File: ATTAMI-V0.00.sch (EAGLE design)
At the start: 25 parts, among them U1 MIC5225, U2 ATTINY85-20SU, U3 1117

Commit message: a versin without the fancy LDO and SOT0232 for the X1117
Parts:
- removed COIN_CELL_(+): (no value), ATtami:PINHD-1X1
- removed D5: Schottky, ATtami:SCHOTTKY-DIODESOD-323
- removed U1: MIC5225, ATtami:V_REG_LDOSMD
- U3: device ATtami:XXX1117 -> ATtami:XXX1117SOT-232
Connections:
- removed net N$4: COIN_CELL_(+).1, D5.A
- net GND: no longer U1.GND
- net VCC: no longer D5.C, U1.OUT
- net V_BAT: no longer U1.EN, U1.IN
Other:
- note added: "Notes: 1. profit!! 2. Cut jumper SJ1 in order to save battery energy. 3. Switch possition of midi jumper and dissable the RESET function in order to use PB5 as DP USB signal. 4. D1 and D2 are Blue LEDs their forward voltage is 3.2V. They might not light when using coin cell or low Vi_BAT. 5. When VCC is less than 5V the system clock of the ATTINY85 should be 8MHz or less (refer to the datasheet P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"
- note added: "this is/was coincell +"
- note removed: "* See Note 1"
- note removed: "Notes: 1. Assemble either U1 or U3. (!!! never both of them !!!) 2. Cut jumper SJ1 in order to save battery energy. 3. Switch possition of midi jumper and dissable the RESET function in order to use PB5 as DP USB signal. 4. D1 and D2 are Blue LEDs their forward voltage is 3.2V. They might not light when using coin cell or low Vi_BAT. 5. When VCC is less than 5V the system clock of the ATTINY85 sh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"
- moved on the sheet: U3
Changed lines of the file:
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@@
 <layer number="19" name="Unrouted" color="6" fill="1" visible="no" active="no"/>
 <layer number="20" name="Dimension" color="15" fill="1" visible="no" active="no"/>
-<layer number="21" name="tPlace" color="7" fill="1" visible="no" active="no"/>
-<layer number="22" name="bPlace" color="7" fill="1" visible="no" active="no"/>
+<layer number="21" name="tPlace" color="16" fill="1" visible="no" active="no"/>
+<layer number="22" name="bPlace" color="14" fill="1" visible="no" active="no"/>
 <layer number="23" name="tOrigins" color="15" fill="1" visible="no" active="no"/>
 <layer number="24" name="bOrigins" color="15" fill="1" visible="no" active="no"/>
@@
 <layer number="49" name="Reference" color="7" fill="1" visible="no" active="no"/>
 <layer number="50" name="dxf" color="7" fill="1" visible="no" active="no"/>
-<layer number="51" name="tDocu" color="7" fill="1" visible="no" active="no"/>
+<layer number="51" name="tDocu" color="6" fill="1" visible="no" active="no"/>
 <layer number="52" name="bDocu" color="7" fill="1" visible="no" active="no"/>
 <layer number="53" name="tGND_GNDA" color="7" fill="9" visible="no" active="no"/>
@@
 <part name="R2" library="ATtami" deviceset="RESISTOR" device="0805-RES" value="1K5"/>
 <part name="GND12" library="ATtami" deviceset="GND" device=""/>
-<part name="U1" library="ATtami" deviceset="V_REG_LDO" device="SMD" value="MIC5225"/>
 <part name="U$1" library="ATtami" deviceset="MOUNTINGHOLE" device="2.0" value="MOUNTINGHOLE2.0"/>
 <part name="S1" library="ATtami" deviceset="SWITCH-MOMENTARY-2" device="-SMD-1101NE"/>
@@
 <part name="J1" library="ATtami" deviceset="HEADER-1X7" device="ROUND"/>
 <part name="GND5" library="ATtami" deviceset="GND" device=""/>
-<part name="D5" library="ATtami" deviceset="SCHOTTKY-DIODE" device="SOD-323" value="Schottky"/>
 <part name="SJ1" library="SparkFun-Passives" deviceset="JUMPER-PAD-2-NC_BY_TRACE" device=""/>
-<part name="COIN_CELL_(+)" library="ATtami" deviceset="PINHD-1X1" device=""/>
 <part name="COIN_CELL_(-)" library="ATtami" deviceset="PINHD-1X1" device=""/>
 <part name="U2" library="ATtami" deviceset="ATTINY85-20SU" device=""/>
-<part name="U3" library="ATtami" deviceset="XXX1117" device="" value="1117"/>
+<part name="U3" library="ATtami" deviceset="XXX1117" device="SOT-232" value="1117"/>
 <part name="SJ2" library="SparkFun-Passives" deviceset="JUMPER-PAD-3-2OF3_NC_BY_TRACE" device="_SMALL"/>
 <part name="GND7" library="ATtami" deviceset="GND" device=""/>
@@
 <plain>
 <text x="35.56" y="35.56" size="1.778" layer="100">Notes:
-1. Assemble either U1 or U3. (!!! never both of them !!!)
+1. profit!!
 2. Cut jumper SJ1 in order to save battery energy.
 3. Switch possition of midi jumper and dissable the RESET function in order to use PB5 as DP USB signal.
@@
 <text x="212.344" y="93.218" size="1.778" layer="91" rot="R270">Reset</text>
 <text x="193.802" y="92.71" size="1.778" layer="91">midi jumper</text>
-<text x="75.438" y="143.51" size="1.778" layer="91">* See Note 1</text>
-<text x="74.676" y="121.158" size="1.778" layer="91">* See Note 1</text>
+<text x="76.2" y="165.1" size="1.778" layer="91">this is/was coincell +</text>
 </plain>
 <instances>
@@
 </instance>
 <instance part="GND12" gate="1" x="144.78" y="88.9" rot="R90"/>
-<instance part="U1" gate="G$1" x="78.74" y="111.76" smashed="yes">
-<attribute name="NAME" x="71.12" y="120.904" size="1.778" layer="95"/>
-<attribute name="VALUE" x="68.58" y="100.33" size="1.778" layer="96"/>
-</instance>
 <instance part="U$1" gate="G$1" x="228.6" y="165.1"/>
 <instance part="S1" gate="G$1" x="210.82" y="96.52" smashed="yes" rot="R270"/>
@@
 <instance part="J1" gate="A" x="231.14" y="111.76"/>
 <instance part="GND5" gate="1" x="220.98" y="127" rot="R180"/>
-<instance part="D5" gate="G$1" x="63.5" y="165.1" smashed="yes" rot="R180">
-<attribute name="NAME" x="61.976" y="168.148" size="1.27" layer="95" rot="R180"/>
-<attribute name="VALUE" x="68.072" y="163.068" size="1.27" layer="96" rot="R180"/>
-</instance>
 <instance part="SJ1" gate="G$1" x="134.62" y="88.9" smashed="yes" rot="R180">
 <attribute name="NAME" x="137.16" y="92.71" size="1.778" layer="95" rot="R180"/>
-</instance>
-<instance part="COIN_CELL_(+)" gate="G$1" x="81.28" y="165.1" smashed="yes">
-<attribute name="NAME" x="83.82" y="164.719" size="1.778" layer="95"/>
-<attribute name="VALUE" x="74.93" y="160.02" size="1.778" layer="96"/>
 </instance>
 <instance part="COIN_CELL_(-)" gate="G$1" x="81.28" y="154.94" smashed="yes">
@@
 <attribute name="VALUE" x="159.1564" y="94.361" size="2.0828" layer="96" ratio="10" rot="SR0"/>
 </instance>
-<instance part="U3" gate="1" x="76.2" y="139.7" smashed="yes">
-<attribute name="NAME" x="71.12" y="143.256" size="1.778" layer="95"/>
-<attribute name="VALUE" x="69.596" y="131.826" size="1.778" layer="96"/>
+<instance part="U3" gate="1" x="78.74" y="116.84" smashed="yes">
+<attribute name="NAME" x="73.66" y="120.396" size="1.778" layer="95"/>
+<attribute name="VALUE" x="72.136" y="108.966" size="1.778" layer="96"/>
 </instance>
 <instance part="SJ2" gate="G$1" x="193.04" y="96.52" smashed="yes" rot="MR90"/>
-<instance part="GND7" gate="1" x="76.2" y="127" smashed="yes">
-<attribute name="VALUE" x="73.66" y="124.46" size="1.778" layer="96"/>
+<instance part="GND7" gate="1" x="78.74" y="104.14" smashed="yes">
+<attribute name="VALUE" x="76.2" y="101.6" size="1.778" layer="96"/>
 </instance>
 </instances>
@@
 <wire x1="93.98" y1="101.6" x2="93.98" y2="91.44" width="0.1524" layer="91"/>
 <wire x1="66.04" y1="91.44" x2="93.98" y2="91.44" width="0.1524" layer="91"/>
-<wire x1="66.04" y1="91.44" x2="66.04" y2="111.76" width="0.1524" layer="91"/>
-<pinref part="U1" gate="G$1" pin="GND"/>
-<wire x1="66.04" y1="111.76" x2="68.58" y2="111.76" width="0.1524" layer="91"/>
 </segment>
 <segment>
@@
 <pinref part="U3" gate="1" pin="GND"/>
 <pinref part="GND7" gate="1" pin="GND"/>
-<wire x1="76.2" y1="132.08" x2="76.2" y2="129.54" width="0.1524" layer="91"/>
+<wire x1="78.74" y1="109.22" x2="78.74" y2="106.68" width="0.1524" layer="91"/>
 </segment>
 </net>
@@
 <segment>
 <pinref part="U3" gate="1" pin="IN"/>
-<wire x1="68.58" y1="139.7" x2="63.5" y2="139.7" width="0.1524" layer="91"/>
 <pinref part="J2" gate="G$1" pin="1"/>
-<pinref part="U1" gate="G$1" pin="IN"/>
-<wire x1="63.5" y1="116.84" x2="68.58" y2="116.84" width="0.1524" layer="91"/>
-<junction x="63.5" y="116.84"/>
-<pinref part="U1" gate="G$1" pin="EN"/>
-<wire x1="68.58" y1="106.68" x2="63.5" y2="106.68" width="0.1524" layer="91"/>
-<wire x1="63.5" y1="106.68" x2="63.5" y2="116.84" width="0.1524" layer="91"/>
 <pinref part="C1" gate="G$1" pin="1"/>
 <wire x1="50.8" y1="109.22" x2="50.8" y2="116.84" width="0.1524" layer="91"/>
-<wire x1="50.8" y1="116.84" x2="63.5" y2="116.84" width="0.1524" layer="91"/>
+<wire x1="50.8" y1="116.84" x2="71.12" y2="116.84" width="0.1524" layer="91"/>
 <junction x="50.8" y="116.84"/>
 <wire x1="50.8" y1="116.84" x2="40.64" y2="116.84" width="0.1524" layer="91"/>
 <label x="51.816" y="117.856" size="1.778" layer="95"/>
-<junction x="63.5" y="116.84"/>
-<wire x1="63.5" y1="116.84" x2="63.5" y2="139.7" width="0.1524" layer="91"/>
 </segment>
 </net>
@@
 <wire x1="127" y1="111.76" x2="127" y2="116.84" width="0.1524" layer="91"/>
 <junction x="127" y="116.84"/>
-<pinref part="U1" gate="G$1" pin="OUT"/>
 <wire x1="106.68" y1="116.84" x2="93.98" y2="116.84" width="0.1524" layer="91"/>
 <pinref part="U2" gate="A" pin="VCC"/>
 <junction x="144.78" y="116.84"/>
 <pinref part="U3" gate="1" pin="OUT"/>
-<wire x1="93.98" y1="116.84" x2="86.36" y2="116.84" width="0.1524" layer="91"/>
-<wire x1="83.82" y1="139.7" x2="93.98" y2="139.7" width="0.1524" layer="91"/>
-<wire x1="93.98" y1="139.7" x2="93.98" y2="116.84" width="0.1524" layer="91"/>
+<wire x1="86.36" y1="116.84" x2="93.98" y2="116.84" width="0.1524" layer="91"/>
 <junction x="93.98" y="116.84"/>
 </segment>
 <segment>
-<pinref part="D5" gate="G$1" pin="C"/>
-<wire x1="60.96" y1="165.1" x2="55.88" y2="165.1" width="0.1524" layer="91"/>
 <wire x1="55.88" y1="165.1" x2="55.88" y2="160.02" width="0.1524" layer="91"/>
 <pinref part="J3" gate="G$1" pin="1"/>
 <wire x1="55.88" y1="160.02" x2="38.1" y2="160.02" width="0.1524" layer="91"/>
 <label x="46.228" y="160.528" size="1.778" layer="95"/>
+<wire x1="55.88" y1="165.1" x2="78.74" y2="165.1" width="0.1524" layer="91"/>
 </segment>
 </net>
@@
 </segment>
 </net>
-<net name="N$4" class="0">
-<segment>
-<pinref part="D5" gate="G$1" pin="A"/>
-<pinref part="COIN_CELL_(+)" gate="G$1" pin="1"/>
-<wire x1="66.04" y1="165.1" x2="78.74" y2="165.1" width="0.1524" layer="91"/>
-</segment>
-</net>

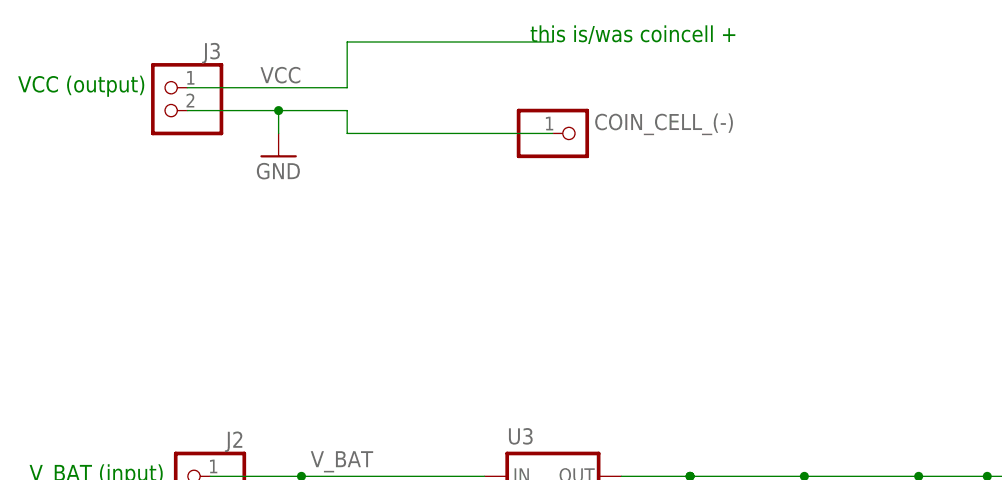
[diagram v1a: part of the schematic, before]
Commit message: moved power led jumper to top layer
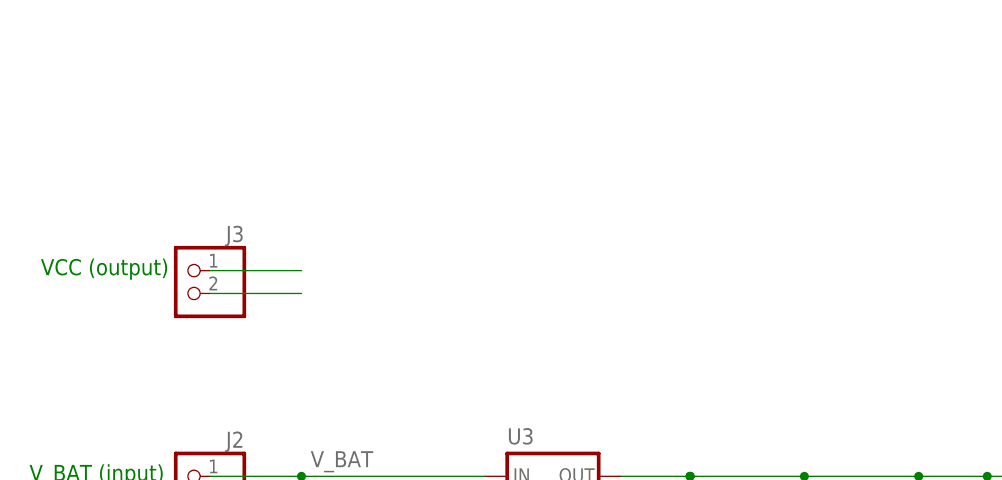
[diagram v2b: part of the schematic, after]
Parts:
- removed COIN_CELL_(-): (no value), ATtami:PINHD-1X1
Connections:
- net GND: no longer COIN_CELL_(-).1
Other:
- note removed: "this is/was coincell +"
- moved on the sheet: J3
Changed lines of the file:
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@@
 <?xml version="1.0" encoding="utf-8"?>
 <!DOCTYPE eagle SYSTEM "eagle.dtd">
-<eagle version="7.2.0">
+<eagle version="7.1.0">
 <drawing>
 <settings>
@@
 <part name="D1" library="ATtami" deviceset="LED" device="-0805" value="Blue LED"/>
 <part name="D2" library="ATtami" deviceset="LED" device="-0805" value="Blue LED"/>
-<part name="GND16" library="ATtami" deviceset="GND" device=""/>
 <part name="GND13" library="ATtami" deviceset="GND" device=""/>
 <part name="GND1" library="ATtami" deviceset="GND" device=""/>
@@
 <part name="GND5" library="ATtami" deviceset="GND" device=""/>
 <part name="SJ1" library="SparkFun-Passives" deviceset="JUMPER-PAD-2-NC_BY_TRACE" device=""/>
-<part name="COIN_CELL_(-)" library="ATtami" deviceset="PINHD-1X1" device=""/>
 <part name="U2" library="ATtami" deviceset="ATTINY85-20SU" device=""/>
 <part name="U3" library="ATtami" deviceset="XXX1117" device="SOT-232" value="1117"/>
@@
 <text x="165.1" y="12.7" size="2.54" layer="100" font="vector">T.A.M.I hackerspace crew
 LICENSE: CERN OHL 1.7</text>
-<text x="19.304" y="159.512" size="1.778" layer="91">VCC (output)</text>
+<text x="21.844" y="139.192" size="1.778" layer="91">VCC (output)</text>
 <text x="20.574" y="116.332" size="1.778" layer="91">V_BAT (input)</text>
 <text x="212.344" y="93.218" size="1.778" layer="91" rot="R270">Reset</text>
 <text x="193.802" y="92.71" size="1.778" layer="91">midi jumper</text>
-<text x="76.2" y="165.1" size="1.778" layer="91">this is/was coincell +</text>
 </plain>
 <instances>
@@
 <instance part="D1" gate="LED" x="106.68" y="66.04"/>
 <instance part="D2" gate="LED" x="119.38" y="66.04"/>
-<instance part="GND16" gate="1" x="48.26" y="152.4"/>
 <instance part="GND13" gate="1" x="210.82" y="86.36"/>
 <instance part="GND1" gate="1" x="43.18" y="104.14"/>
@@
 <instance part="U$2" gate="G$1" x="241.3" y="165.1"/>
 <instance part="J2" gate="G$1" x="38.1" y="114.3" rot="MR0"/>
-<instance part="J3" gate="G$1" x="35.56" y="157.48" rot="MR0"/>
+<instance part="J3" gate="G$1" x="38.1" y="137.16" rot="MR0"/>
 <instance part="FRAME1" gate="G$1" x="0" y="0"/>
 <instance part="J1" gate="A" x="231.14" y="111.76"/>
@@
 <instance part="SJ1" gate="G$1" x="134.62" y="88.9" smashed="yes" rot="R180">
 <attribute name="NAME" x="137.16" y="92.71" size="1.778" layer="95" rot="R180"/>
-</instance>
-<instance part="COIN_CELL_(-)" gate="G$1" x="81.28" y="154.94" smashed="yes">
-<attribute name="NAME" x="83.312" y="155.321" size="1.778" layer="95"/>
-<attribute name="VALUE" x="74.93" y="149.86" size="1.778" layer="96"/>
 </instance>
 <instance part="U2" gate="A" x="162.56" y="114.3" smashed="yes">
@@
 </segment>
 <segment>
-<pinref part="GND16" gate="1" pin="GND"/>
-<wire x1="48.26" y1="157.48" x2="48.26" y2="154.94" width="0.1524" layer="91"/>
-<pinref part="J3" gate="G$1" pin="2"/>
-<wire x1="48.26" y1="157.48" x2="38.1" y2="157.48" width="0.1524" layer="91"/>
-<wire x1="78.74" y1="154.94" x2="55.88" y2="154.94" width="0.1524" layer="91"/>
-<wire x1="55.88" y1="154.94" x2="55.88" y2="157.48" width="0.1524" layer="91"/>
-<wire x1="55.88" y1="157.48" x2="48.26" y2="157.48" width="0.1524" layer="91"/>
-<junction x="48.26" y="157.48"/>
-<pinref part="COIN_CELL_(-)" gate="G$1" pin="1"/>
-</segment>
-<segment>
 <pinref part="GND6" gate="1" pin="GND"/>
 <pinref part="C1" gate="G$1" pin="2"/>
@@
 <pinref part="GND7" gate="1" pin="GND"/>
 <wire x1="78.74" y1="109.22" x2="78.74" y2="106.68" width="0.1524" layer="91"/>
+</segment>
+<segment>
+<pinref part="J3" gate="G$1" pin="2"/>
+<wire x1="40.64" y1="137.16" x2="50.8" y2="137.16" width="0.1524" layer="91"/>
 </segment>
 </net>
@@
 </segment>
 <segment>
-<wire x1="55.88" y1="165.1" x2="55.88" y2="160.02" width="0.1524" layer="91"/>
 <pinref part="J3" gate="G$1" pin="1"/>
-<wire x1="55.88" y1="160.02" x2="38.1" y2="160.02" width="0.1524" layer="91"/>
-<label x="46.228" y="160.528" size="1.778" layer="95"/>
-<wire x1="55.88" y1="165.1" x2="78.74" y2="165.1" width="0.1524" layer="91"/>
-</segment>
-</net>
+<wire x1="40.64" y1="139.7" x2="50.8" y2="139.7" width="0.1524" layer="91"/>
+</segment>
+</net>

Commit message: gerbering to fab
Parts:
- removed U3: 1117, ATtami:XXX1117SOT-232
- added U1: ATTINY85-20SU, ATtami:ATTINY85-20SU
- U2: value ATTINY85-20SU -> (none); device ATtami:ATTINY85-20SU -> ATtami:XXX1117SOT-232
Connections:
- net GND: now also U1.GND; no longer U3.GND
- net PB0: now also U1.PB0; no longer U2.PB0
- net PB1: now also U1.PB1; no longer U2.PB1
- net PB2: now also U1.PB2; no longer U2.PB2
- net PB3: now also U1.PB3; no longer U2.PB3
- net PB4: now also U1.PB4; no longer U2.PB4
- net PB5: now also U1.PB5; no longer U2.PB5
- net VCC: now also U1.VCC, U2.OUT; no longer U2.VCC, U3.OUT
- net V_BAT: now also U2.IN; no longer U3.IN
